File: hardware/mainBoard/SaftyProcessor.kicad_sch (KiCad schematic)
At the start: 24 parts, among them J1 1935161, J7 Conn_02x06_Odd_Even, U1 TCMT1109, U2 TCMT1109, U3 TCMT1109

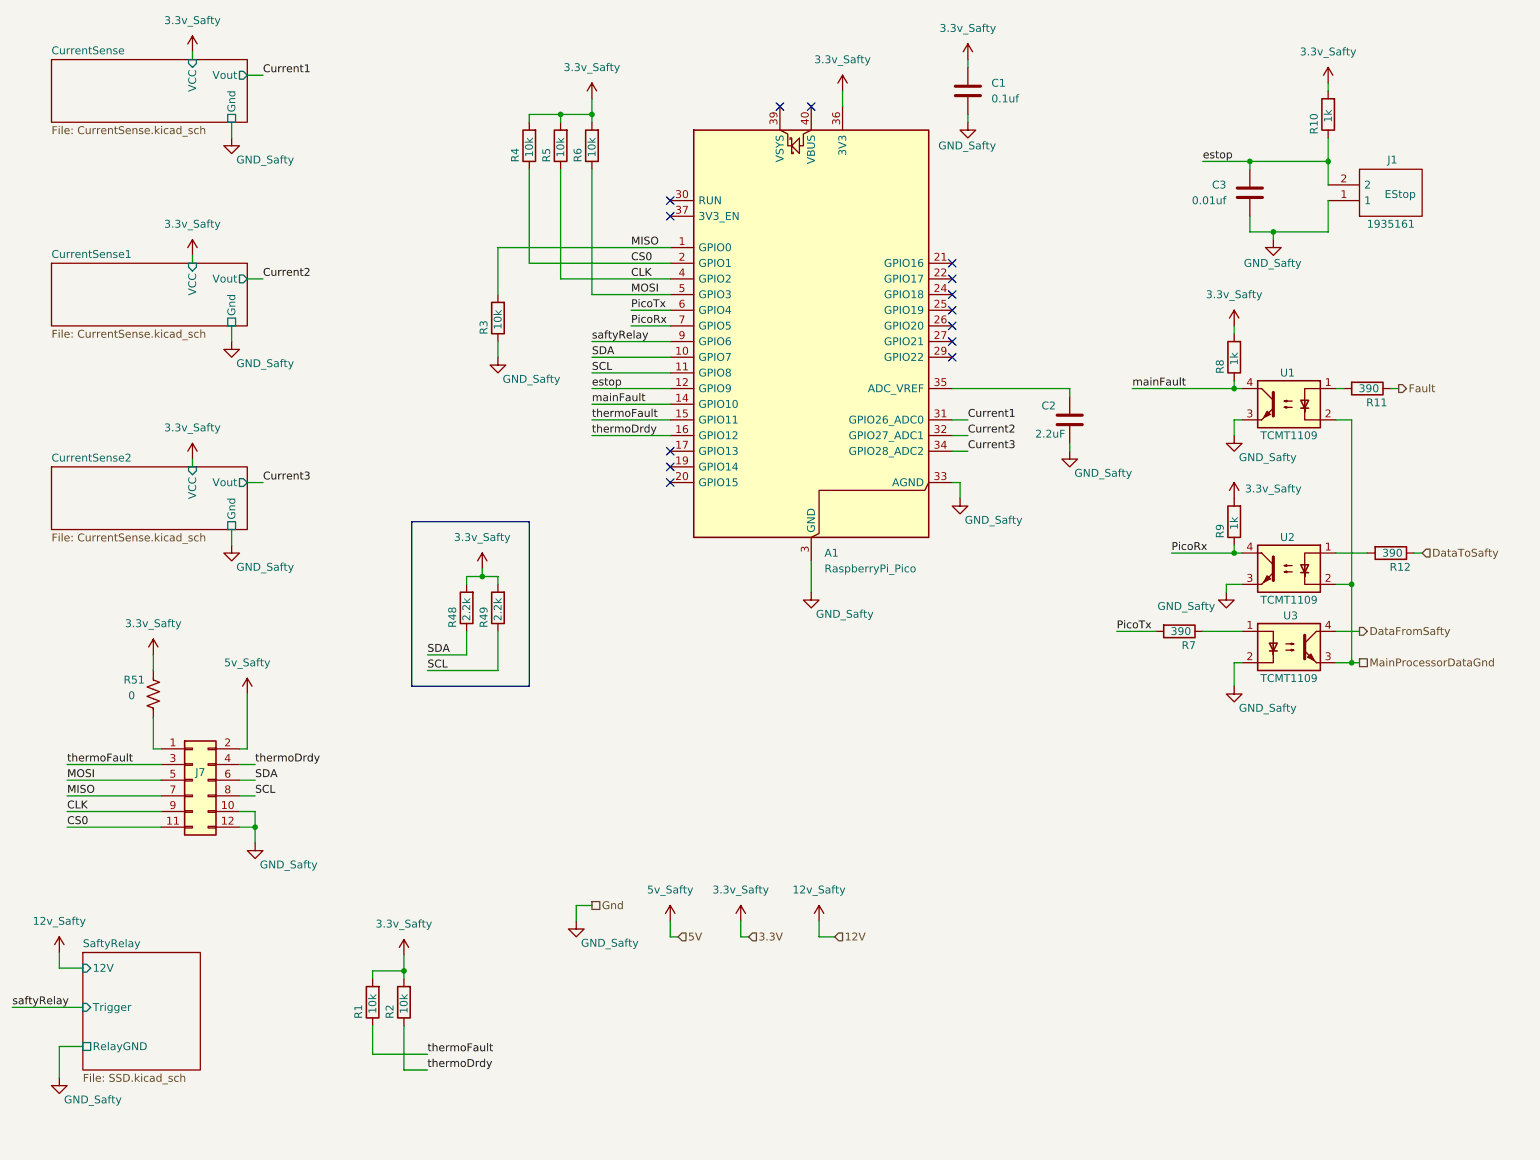
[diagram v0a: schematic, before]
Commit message: Safety link: ADuM1201 replaces the optocouplers, and 9600 was never our limit
The TCMT1109 pair (U2/U3 with R7/R12/R15) that carried the ESP<->RP2040
UART is gone, replaced by one ADuM1201WT digital isolator, U6. Two
properties of that part drove every firmware change here:

  - It does not invert. Each optocoupler did, which is why both ends
    inverted their own TX to cancel it. With a non-inverting barrier
    those cancellations have nothing to cancel, so keeping either one
    parks the far end's RX in a permanent break. Measured with the
    isolator fitted and the old inversions still in place: sent 18,
    received 0, crc/framing errors 33 and climbing, Pico RX pad low on
    2954 of 3000 samples. Both inversions removed:
    uart_set_line_inverse(TXD_INV) from safety_link.c and
    gpio_set_outover(GPIO_OVERRIDE_INVERT) from uart_owner.c.

  - It is fast. The 9600 ceiling was a property of the optocouplers, not
    of either firmware, and every doc that said otherwise was wrong.
    A descending sweep of the standard rates, 60s continuous per rate,
    judged on crc/framing + length-mismatch + crc-mismatch + resync
    deltas: 921600, 460800 and 230400 all clean, zero new errors, status
    replies answering every 500ms poll. Committed value is 230400 -- one
    standard step below the fastest pass is 460800, and 230400 is the
    slower of that and the requested 230400. Two full standard steps of
    margin below a rate that soaks clean.

Also found, while reading the code this change touches: the bootloader's
recovery mode never applied the TX inversion the application did, and its
comment claimed the two matched. Under the optocouplers recovery mode's
Pico->ESP polarity was therefore inverted relative to the application.
Both are non-inverting now, so recovery mode is correct for the first
time -- documented in bootloader/main.c rather than silently fixed.

Baud is hardcoded in three places that must agree, now called out in each:
KilnFW's KILNCTL_SAFET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
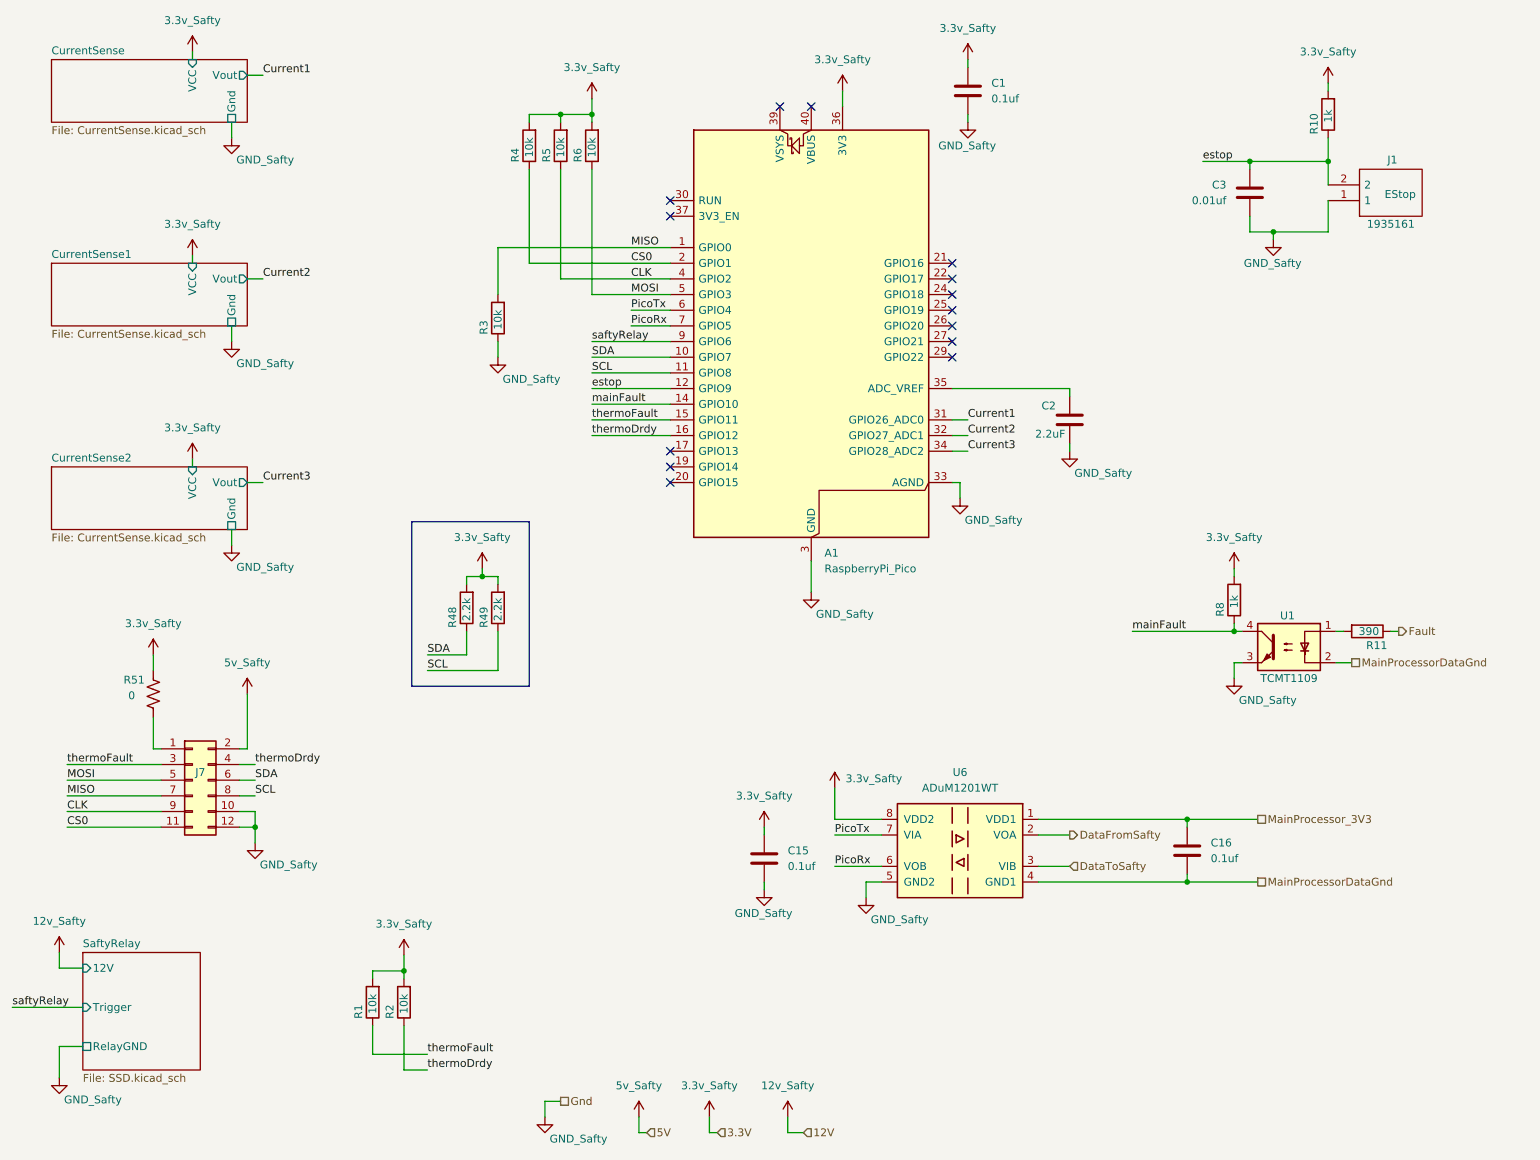
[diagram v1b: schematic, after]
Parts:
- removed R12, R7: 390, Resistor_SMD:R_0402_1005Metric, symbol Device:R
- removed R9: 1k, Resistor_SMD:R_0402_1005Metric, symbol Device:R
- removed U2, U3: TCMT1109, Package_SO:SOP-4_4.4x2.6mm_P1.27mm, symbol Isolator:TCMT1109
- added C15, C16: 0.1uf, Capacitor_SMD:C_0402_1005Metric, symbol Device:C
- added U6: ADuM1201WT, Package_SO:SOIC-8_3.9x4.9mm_P1.27mm, symbol Isolator:ADuM1201WT
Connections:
- net 3.3v_Safty: now also C15.1, U6.8 (VDD2)
- net DataFromSafty: now also U6.2 (VOA)
- net DataToSafty: now also U6.3 (VIB)
- net GND_Safty: now also C15.2, U6.5 (GND2)
- net MainProcessorDataGnd: now also C16.2, U6.4 (GND1)
- net PicoRx: now also U6.6 (VOB)
- net PicoTx: now also U6.7 (VIA)
- new net MainProcessor_3V3: C16.1, U6.1 (VDD1)
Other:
- moved on the sheet: R11, R8, U1
